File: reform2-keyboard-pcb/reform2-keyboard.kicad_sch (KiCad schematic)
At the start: 124 parts, among them SW1 Choc, SW10 Choc, SW11 Choc, SW13 Choc, SW14 Choc, SW15 Choc, SW16 Choc, SW17 Choc, SW19 Choc, SW2 Choc, SW20 Choc, SW21 Choc, SW22 Choc, SW23 Choc, SW25 Choc, SW26 Choc, SW27 Choc, SW28 Choc, SW29 Choc, SW3 Choc, SW31 Choc, SW32 Choc, SW33 Choc, SW34 Choc, SW35 Choc, SW37 Choc, SW38 Choc, SW39 Choc, SW4 Choc, SW40 Choc, SW41 Choc, SW43 Choc, SW44 Choc, SW45 Choc, SW46 Choc, SW47 Choc, SW49 Choc, SW5 Choc, SW50 Choc, SW51 Choc, SW52 Choc, SW53 Choc, SW55 Choc, SW56 Choc, SW57 Choc, SW58 Choc, SW59 Choc, SW61 Choc, SW62 Choc, SW63 Choc, SW64 Choc, SW65 Choc, SW67 Choc, SW68 Choc, SW69 Choc, SW7 Choc, SW70 Choc, SW71 Choc, SW72 Choc, SW73 Choc, SW8 Choc, SW9 Choc

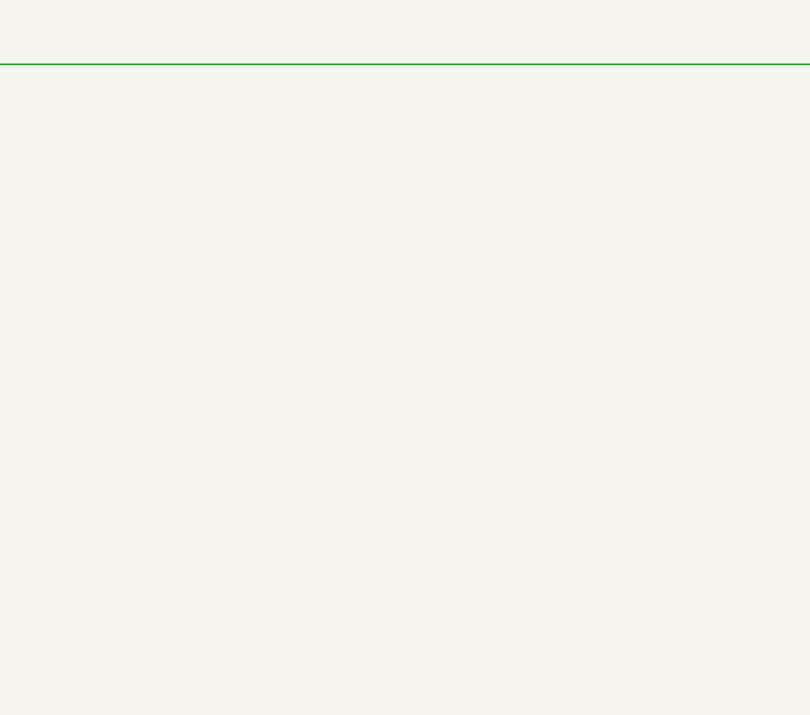
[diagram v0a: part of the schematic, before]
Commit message: more routing of smd parts, add sockets
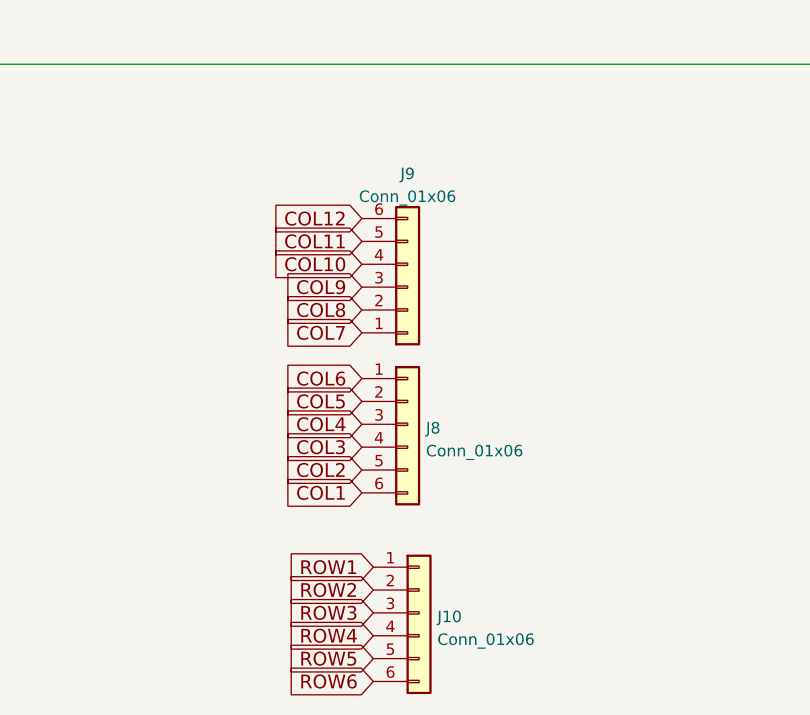
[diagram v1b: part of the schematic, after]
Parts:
- added J10, J8, J9: Conn_01x06, Connector_PinHeader_2.54mm:PinHeader_1x06_P2.54mm_Vertical, symbol Connector_Generic:Conn_01x06
- SW10, SW11, SW14, SW15, SW16, SW17, SW19, SW2, SW20, SW21, SW22, SW23, SW25, SW26, SW28, SW3, SW31, SW32, SW33, SW34, SW37, SW38, SW39, SW4, SW40, SW43, SW44, SW46, SW49, SW5, SW50, SW51, SW52, SW53, SW56, SW57, SW58, SW59, SW62, SW63, SW64, SW65, SW68, SW69, SW70, SW71, SW8, SW9: footprint keyswitches:PG1350 -> keyswitches:PG1350_optional-socket
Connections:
- net COL1: now also J8.6 (Pin_6)
- net COL10: now also J9.4 (Pin_4)
- net COL11: now also J9.5 (Pin_5)
- net COL12: now also J9.6 (Pin_6)
- net COL2: now also J8.5 (Pin_5)
- net COL3: now also J8.4 (Pin_4)
- net COL4: now also J8.3 (Pin_3)
- net COL5: now also J8.2 (Pin_2)
- net COL6: now also J8.1 (Pin_1)
- net COL7: now also J9.1 (Pin_1)
- net COL8: now also J9.2 (Pin_2)
- net COL9: now also J9.3 (Pin_3)
- net ROW1: now also J10.1 (Pin_1)
- net ROW2: now also J10.2 (Pin_2)
- net ROW3: now also J10.3 (Pin_3)
- net ROW4: now also J10.4 (Pin_4)
- net ROW5: now also J10.5 (Pin_5)
- net ROW6: now also J10.6 (Pin_6)

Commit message: change parts for better handsolders
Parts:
- D1, D10, D11, D13, D14, D15, D16, D17, D19, D2, D20, D21, D22, D23, D25, D26, D27, D28, D29, D3, D31, D32, D33, D34, D35, D37, D38, D39, D4, D40, D41, D43, D44, D45, D46, D47, D49, D5, D50, D51, D52, D53, D55, D56, D57, D58, D59, D61, D62, D63, D64, D65, D67, D68, D69, D7, D70, D71, D72, D73, D8, D9: footprint Diode_SMD:D_0603_1608Metric_Pad1.05x0.95mm_HandSolder -> Diode_SMD:D_SOD-123
